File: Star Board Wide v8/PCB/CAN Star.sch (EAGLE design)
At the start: 24 parts

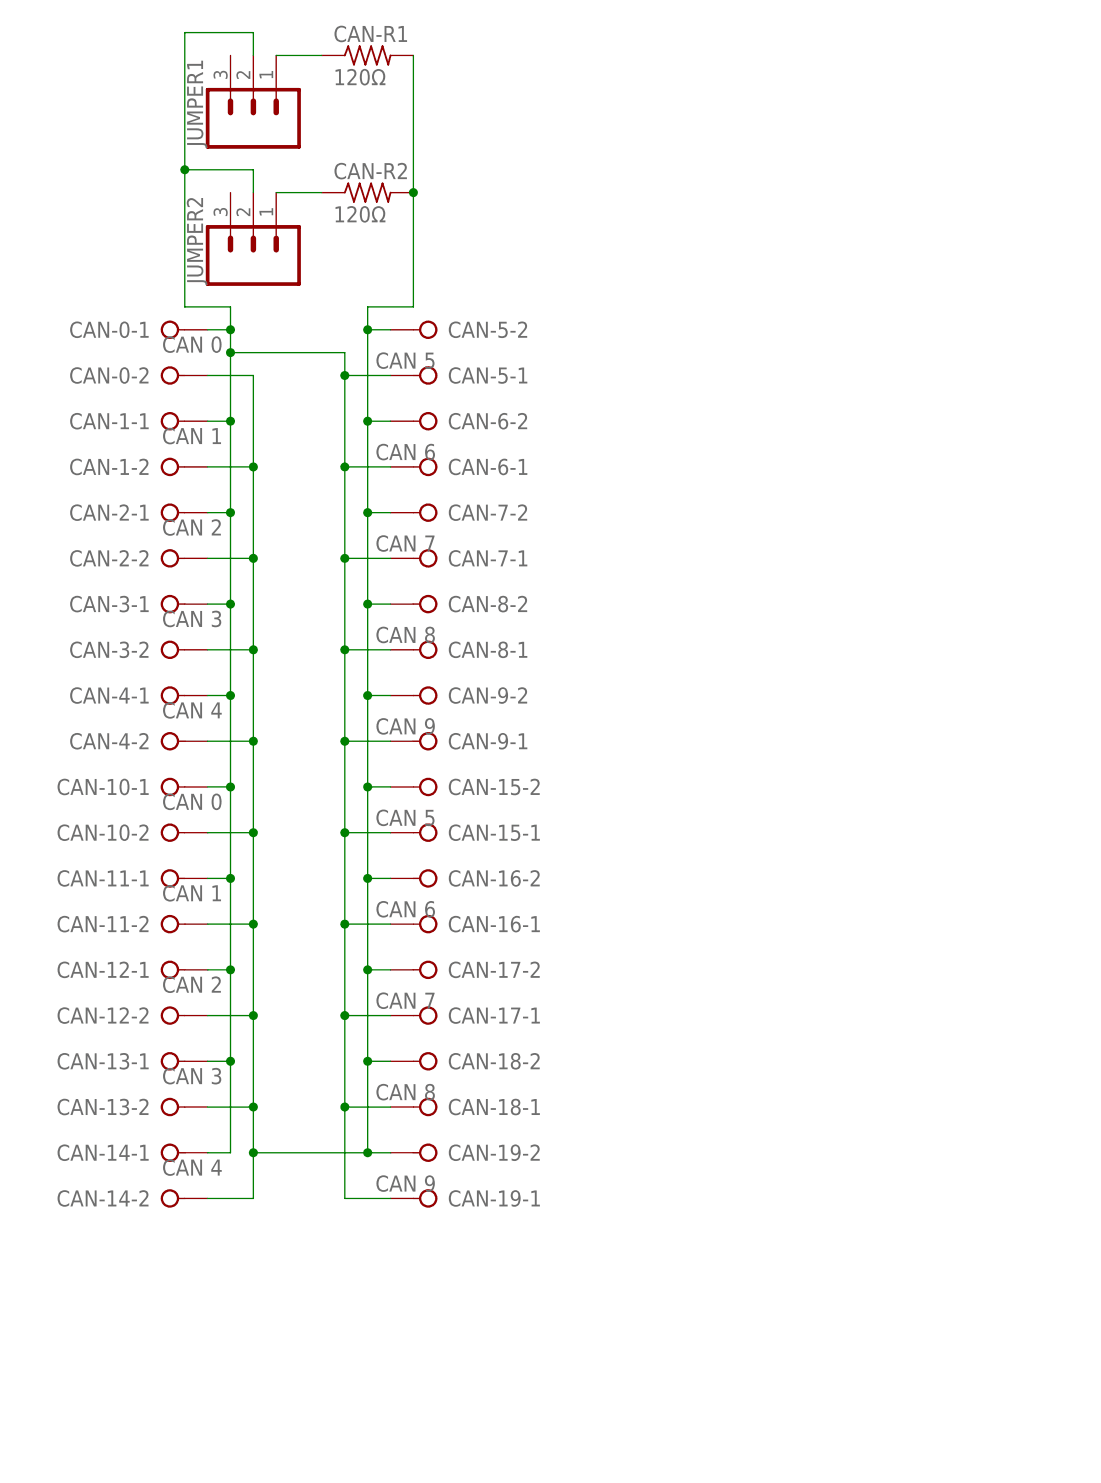
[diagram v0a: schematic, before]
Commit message: switch to wide-v9, add in grounds, removed odd connections, needs layout work
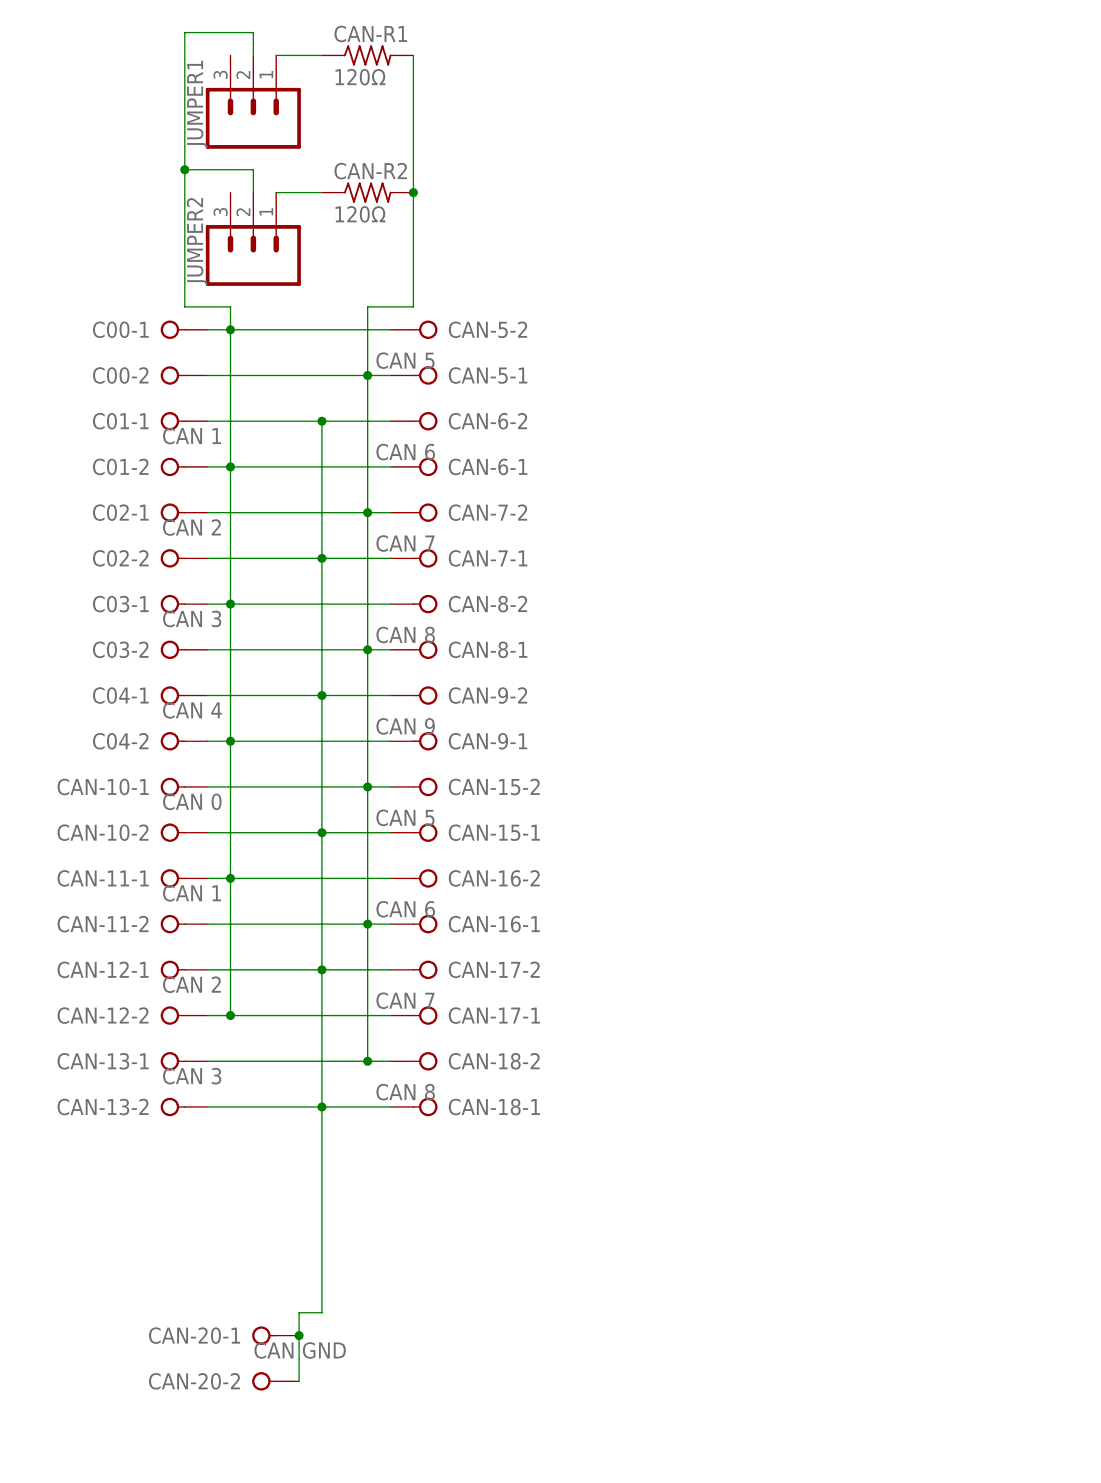
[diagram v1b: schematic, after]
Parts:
- removed CAN-14: CAN 4, con-wago-508:W237-02P
- removed CAN-19: CAN 9, con-wago-508:W237-02P
- added CAN-20: CAN GND, con-wago-508:W237-02P
- C00: value CAN 0 -> (none)
- renumbered CAN-0 to C00, CAN-1 to C01, CAN-2 to C02, CAN-3 to C03, CAN-4 to C04
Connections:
- removed net CAN-A: C00-1.KL, C01-1.KL, C02-1.KL, C03-1.KL, C04-1.KL, CAN-10-1.KL, CAN-11-1.KL, CAN-12-1.KL, CAN-13-1.KL, CAN-14-1.KL, CAN-15-1.KL, CAN-16-1.KL, CAN-17-1.KL, CAN-18-1.KL, CAN-19-1.KL, CAN-5-1.KL, CAN-6-1.KL, CAN-7-1.KL, CAN-8-1.KL, CAN-9-1.KL, JUMPER1.2, JUMPER2.2
- removed net CAN-B: C00-2.KL, C01-2.KL, C02-2.KL, C03-2.KL, C04-2.KL, CAN-10-2.KL, CAN-11-2.KL, CAN-12-2.KL, CAN-13-2.KL, CAN-14-2.KL, CAN-15-2.KL, CAN-16-2.KL, CAN-17-2.KL, CAN-18-2.KL, CAN-19-2.KL, CAN-5-2.KL, CAN-6-2.KL, CAN-7-2.KL, CAN-8-2.KL, CAN-9-2.KL, CAN-R1.2, CAN-R2.2
- new net G: C00-2.KL, C02-1.KL, C03-2.KL, CAN-10-1.KL, CAN-11-2.KL, CAN-13-1.KL, CAN-15-2.KL, CAN-16-1.KL, CAN-18-2.KL, CAN-5-1.KL, CAN-7-2.KL, CAN-8-1.KL, CAN-R1.2, CAN-R2.2
- new net GND: C01-1.KL, C02-2.KL, C04-1.KL, CAN-10-2.KL, CAN-12-1.KL, CAN-13-2.KL, CAN-15-1.KL, CAN-17-2.KL, CAN-18-1.KL, CAN-20-1.KL, CAN-20-2.KL, CAN-6-2.KL, CAN-7-1.KL, CAN-9-2.KL
- new net Y: C00-1.KL, C01-2.KL, C03-1.KL, C04-2.KL, CAN-11-1.KL, CAN-12-2.KL, CAN-16-2.KL, CAN-17-1.KL, CAN-5-2.KL, CAN-6-1.KL, CAN-8-2.KL, CAN-9-1.KL, JUMPER1.2, JUMPER2.2

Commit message: change layout to 3 by 4
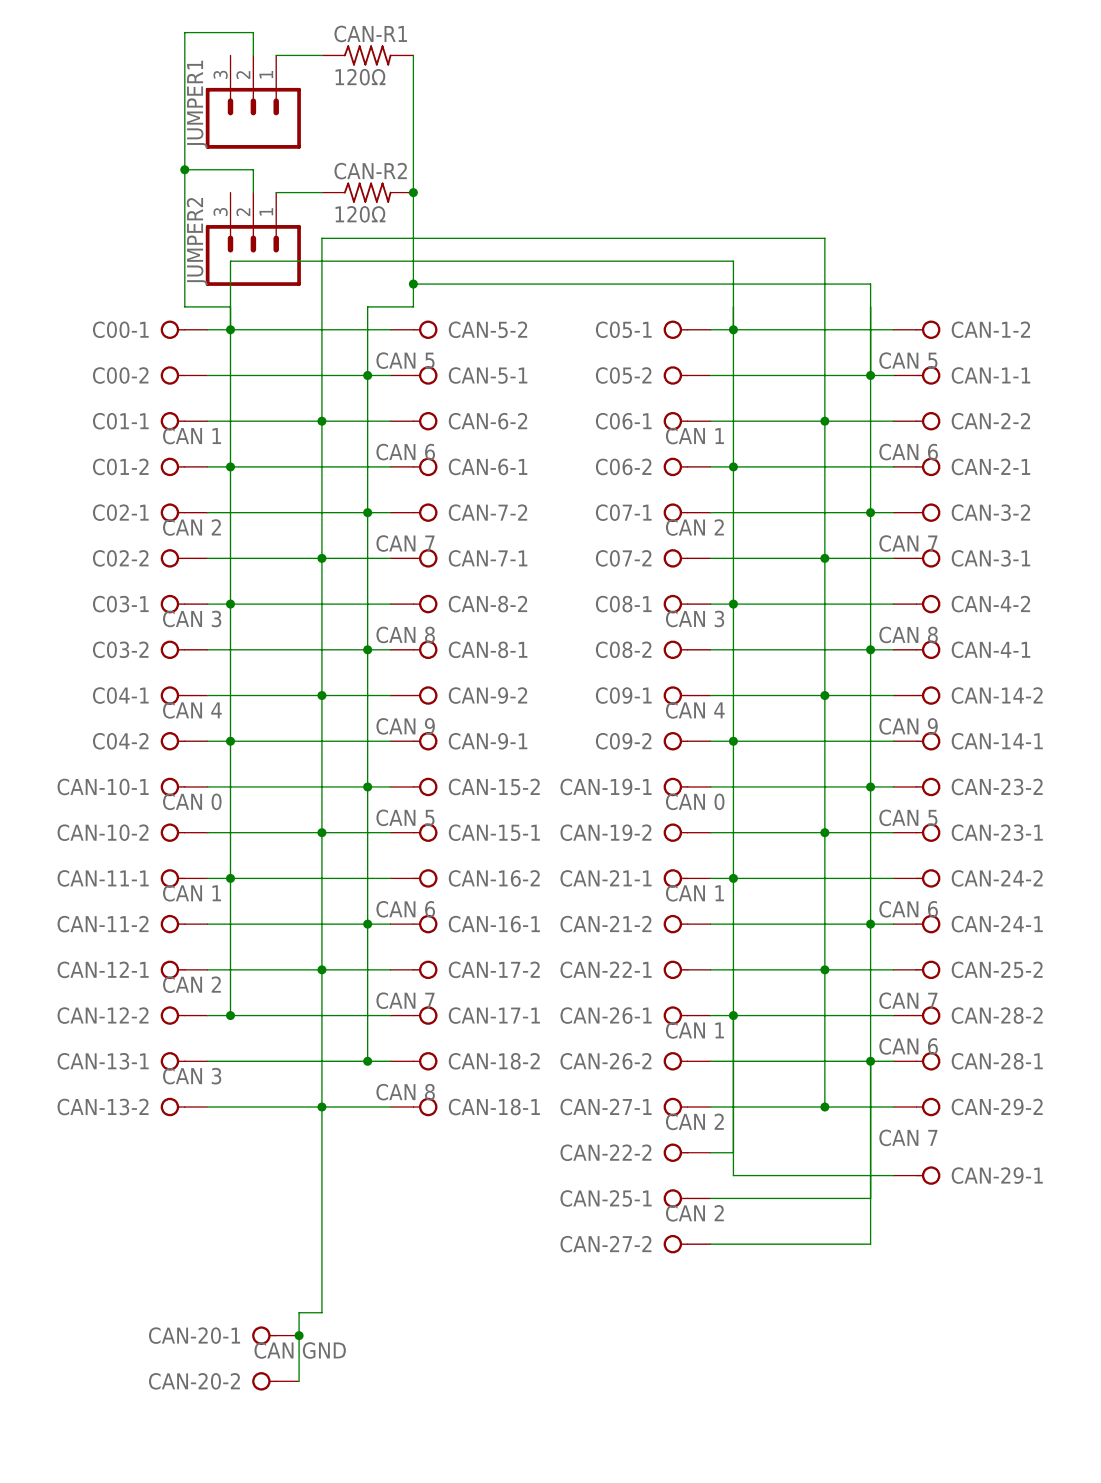
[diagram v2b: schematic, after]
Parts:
- added C05: (no value), con-wago-508:W237-02P
- added C06, CAN-21, CAN-26: CAN 1, con-wago-508:W237-02P
- added C07, CAN-22, CAN-27: CAN 2, con-wago-508:W237-02P
- added C08: CAN 3, con-wago-508:W237-02P
- added C09: CAN 4, con-wago-508:W237-02P
- added CAN-1, CAN-23: CAN 5, con-wago-508:W237-02P
- added CAN-14: CAN 9, con-wago-508:W237-02P
- added CAN-19: CAN 0, con-wago-508:W237-02P
- added CAN-2, CAN-24, CAN-28: CAN 6, con-wago-508:W237-02P
- added CAN-25, CAN-29, CAN-3: CAN 7, con-wago-508:W237-02P
- added CAN-4: CAN 8, con-wago-508:W237-02P
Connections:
- net G: now also C05-2.KL, C07-1.KL, C08-2.KL, CAN-1-1.KL, CAN-19-1.KL, CAN-21-2.KL, CAN-23-2.KL, CAN-24-1.KL, CAN-25-1.KL, CAN-26-2.KL, CAN-27-2.KL, CAN-28-1.KL, CAN-3-2.KL, CAN-4-1.KL
- net GND: now also C06-1.KL, C07-2.KL, C09-1.KL, CAN-14-2.KL, CAN-19-2.KL, CAN-2-2.KL, CAN-22-1.KL, CAN-23-1.KL, CAN-25-2.KL, CAN-27-1.KL, CAN-29-2.KL, CAN-3-1.KL
- net Y: now also C05-1.KL, C06-2.KL, C08-1.KL, C09-2.KL, CAN-1-2.KL, CAN-14-1.KL, CAN-2-1.KL, CAN-21-1.KL, CAN-22-2.KL, CAN-24-2.KL, CAN-26-1.KL, CAN-28-2.KL, CAN-29-1.KL, CAN-4-2.KL

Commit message: Remade board wide v9
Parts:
- removed C00, C05: (no value), con-wago-508:W237-02P
- removed C01, C06, CAN-11, CAN-21, CAN-26: CAN 1, con-wago-508:W237-02P
- removed C02, C07, CAN-12, CAN-22, CAN-27: CAN 2, con-wago-508:W237-02P
- removed C03, C08, CAN-13: CAN 3, con-wago-508:W237-02P
- removed C04, C09: CAN 4, con-wago-508:W237-02P
- removed CAN-1, CAN-15, CAN-23, CAN-5: CAN 5, con-wago-508:W237-02P
- removed CAN-10, CAN-19: CAN 0, con-wago-508:W237-02P
- removed CAN-14, CAN-9: CAN 9, con-wago-508:W237-02P
- removed CAN-16, CAN-2, CAN-24, CAN-28, CAN-6: CAN 6, con-wago-508:W237-02P
- removed CAN-17, CAN-25, CAN-29, CAN-3, CAN-7: CAN 7, con-wago-508:W237-02P
- removed CAN-18, CAN-4, CAN-8: CAN 8, con-wago-508:W237-02P
- removed CAN-20: CAN GND, con-wago-508:W237-02P
- removed CAN-R1, CAN-R2: 120Ω, resistor:R-US_0207/10
- removed JUMPER1, JUMPER2: (no value), SparkFun-Connectors:CONN_03
- added U$1, U$10, U$11, U$12, U$2, U$3, U$4, U$5, U$6, U$7, U$8, U$9: 2-3-TERMS, custom:2-3-TERMS
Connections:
- removed net G: C00-2.KL, C02-1.KL, C03-2.KL, C05-2.KL, C07-1.KL, C08-2.KL, CAN-1-1.KL, CAN-10-1.KL, CAN-11-2.KL, CAN-13-1.KL, CAN-15-2.KL, CAN-16-1.KL, CAN-18-2.KL, CAN-19-1.KL, CAN-21-2.KL, CAN-23-2.KL, CAN-24-1.KL, CAN-25-1.KL, CAN-26-2.KL, CAN-27-2.KL, CAN-28-1.KL, CAN-3-2.KL, CAN-4-1.KL, CAN-5-1.KL, CAN-7-2.KL, CAN-8-1.KL, CAN-R1.2, CAN-R2.2
- removed net N$1: CAN-R1.1, JUMPER1.1
- removed net N$2: CAN-R2.1, JUMPER2.1
- removed net Y: C00-1.KL, C01-2.KL, C03-1.KL, C04-2.KL, C05-1.KL, C06-2.KL, C08-1.KL, C09-2.KL, CAN-1-2.KL, CAN-11-1.KL, CAN-12-2.KL, CAN-14-1.KL, CAN-16-2.KL, CAN-17-1.KL, CAN-2-1.KL, CAN-21-1.KL, CAN-22-2.KL, CAN-24-2.KL, CAN-26-1.KL, CAN-28-2.KL, CAN-29-1.KL, CAN-4-2.KL, CAN-5-2.KL, CAN-6-1.KL, CAN-8-2.KL, CAN-9-1.KL, JUMPER1.2, JUMPER2.2
- new net G(L): U$1.G(L)0, U$1.G(L)1, U$10.G(L)0, U$10.G(L)1, U$11.G(L)0, U$11.G(L)1, U$12.G(L)0, U$12.G(L)1, U$2.G(L)0, U$2.G(L)1, U$3.G(L)0, U$3.G(L)1, U$4.G(L)0, U$4.G(L)1, U$5.G(L)0, U$5.G(L)1, U$6.G(L)0, U$6.G(L)1, U$7.G(L)0, U$7.G(L)1, U$8.G(L)0, U$8.G(L)1, U$9.G(L)0, U$9.G(L)1
- new net Y(H): U$1.Y(H)0, U$1.Y(H)1, U$10.Y(H)0, U$10.Y(H)1, U$11.Y(H)0, U$11.Y(H)1, U$12.Y(H)0, U$12.Y(H)1, U$2.Y(H)0, U$2.Y(H)1, U$3.Y(H)0, U$3.Y(H)1, U$4.Y(H)0, U$4.Y(H)1, U$5.Y(H)0, U$5.Y(H)1, U$6.Y(H)0, U$6.Y(H)1, U$7.Y(H)0, U$7.Y(H)1, U$8.Y(H)0, U$8.Y(H)1, U$9.Y(H)0, U$9.Y(H)1
- net GND: now also U$1.GND0, U$1.GND1, U$10.GND0, U$10.GND1, U$11.GND0, U$11.GND1, U$12.GND0, U$12.GND1, U$2.GND0, U$2.GND1, U$3.GND0, U$3.GND1, U$4.GND0, U$4.GND1, U$5.GND0, U$5.GND1, U$6.GND0, U$6.GND1, U$7.GND0, U$7.GND1, U$8.GND0, U$8.GND1, U$9.GND0, U$9.GND1; no longer C01-1.KL, C02-2.KL, C04-1.KL, C06-1.KL, C07-2.KL, C09-1.KL, CAN-10-2.KL, CAN-12-1.KL, CAN-13-2.KL, CAN-14-2.KL, CAN-15-1.KL, CAN-17-2.KL, CAN-18-1.KL, CAN-19-2.KL, CAN-2-2.KL, CAN-20-1.KL, CAN-20-2.KL, CAN-22-1.KL, CAN-23-1.KL, CAN-25-2.KL, CAN-27-1.KL, CAN-29-2.KL, CAN-3-1.KL, CAN-6-2.KL, CAN-7-1.KL, CAN-9-2.KL
